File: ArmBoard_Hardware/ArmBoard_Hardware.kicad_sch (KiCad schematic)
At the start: 129 parts, among them J1 RJ45_LED_Shielded, Q1 T2N7002AK,LM, Q10 T2N7002AK,LM, Q11 T2N7002AK,LM, Q2 BSS138, Q3 BSS138, Q4 AO3401A, Q5 T2N7002AK,LM, Q6 T2N7002AK,LM, Q7 T2N7002AK,LM, Q8 T2N7002AK,LM, Q9 T2N7002AK,LM, SW1 SW_Push, SW10 SW_Push, SW12 SW_SPDT, SW2 SW_Push, SW3 SW_Push, SW4 SW_Push, SW5 SW_Push, SW6 SW_Push, SW7 SW_Push, SW8 SW_Push, SW9 SW_Push, U1 PCF8574, U10 PCF8574, U2 OKI, U3 OKI, U4 ATA6561, U5 Teensy4.1_DEV-16771, U6 74HC00, U7 74LS148, U8 74LS148, U9 PCF8574

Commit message: Changes made based on review
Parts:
- removed Q1, Q10, Q11, Q5, Q6, Q7, Q8, Q9: T2N7002AK,LM, Package_TO_SOT_SMD:SOT-23-3, symbol T2N7002AK_LM:T2N7002AK,LM
- removed R28, R30: 4.7k, Resistor_SMD:R_0603_1608Metric_Pad0.98x0.95mm_HandSolder, symbol Device:R
- added Q1, Q10, Q12, Q5, Q6, Q7, Q8, Q9: BSS138, Package_TO_SOT_SMD:SOT-23, symbol Transistor_FET:BSS138
- C6: value 10nF -> 100nF
- R10, R11, R12, R13, R4, R5, R6, R7, R8, R9: value R -> 4.7k
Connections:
- net GND: now also Q1.2 (S), Q10.2 (S), Q12.2 (S), Q5.2 (S), Q6.2 (S), Q7.2 (S), Q8.2 (S), Q9.2 (S)
- net PWM_1: now also Q12.1 (G)
- net PWM_2: now also Q5.1 (G)
- net PWM_3: now also Q1.1 (G)
- net PWM_4: now also Q6.1 (G)
- net PWM_5: now also Q7.1 (G)
- net PWM_6: now also Q8.1 (G)
- net PWM_7: now also Q9.1 (G)
- net PWM_8: now also Q10.1 (G)
- net at D10.1 (K): now also Q7.3 (D)
- net at D13.1 (K): now also Q10.3 (D)
- net at D12.1 (K): now also Q9.3 (D)
- net at D7.1 (K): now also Q5.3 (D)
- net at D4.1 (K): now also Q12.3 (D)
- net at D9.1 (K): now also Q6.3 (D)
- net at D11.1 (K): now also Q8.3 (D)
- net at D8.1 (K): now also Q1.3 (D)
- no-connect marks 16 -> 20
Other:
- moved on the sheet: Conn22, Conn23, Conn25, Conn26, Conn27, Conn3, R16, R17, R18, R19, R20, R21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

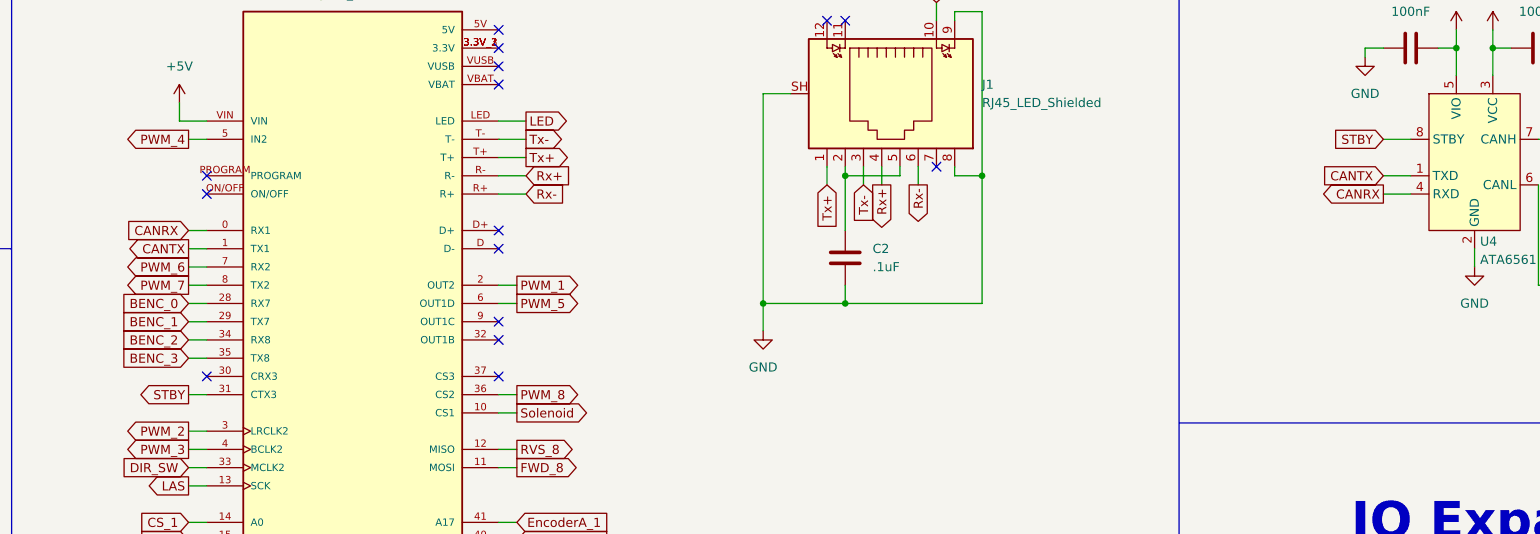
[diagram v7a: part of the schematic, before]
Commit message: Grounded standby on CAN transceiver
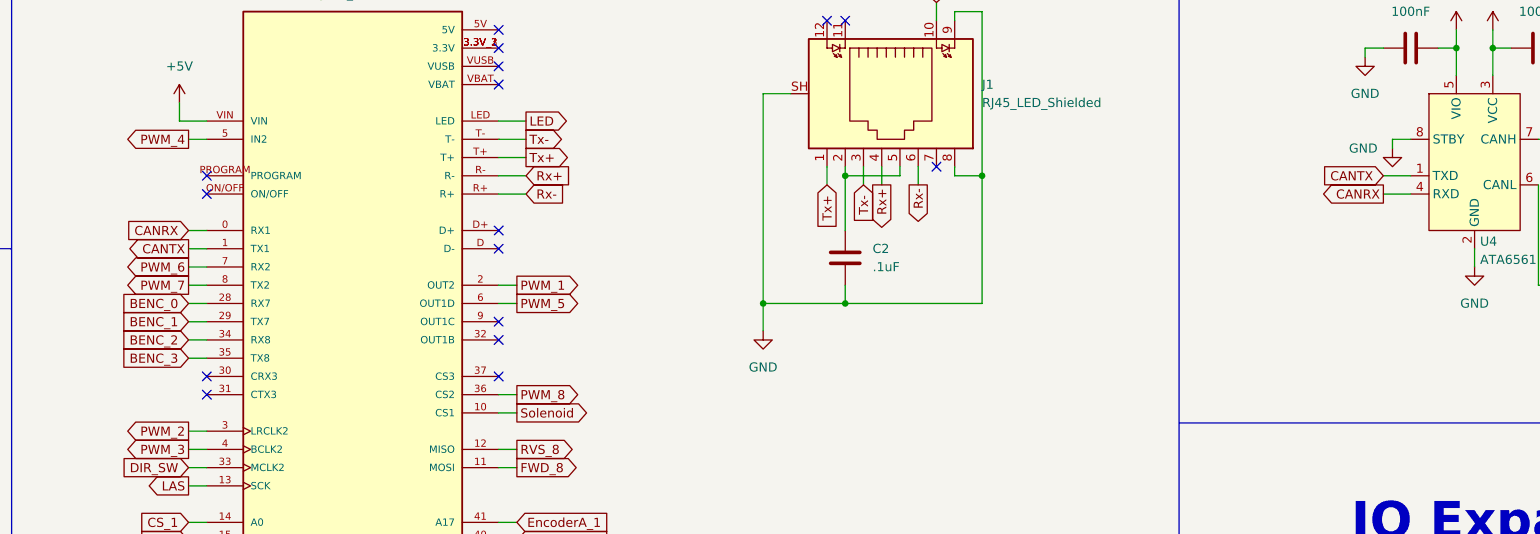
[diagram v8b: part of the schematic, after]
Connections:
- net GND: now also U4.8 (STBY)
- net STBY: no longer names the net of U5.31 (CTX3)
- net STBY: no longer U4.8 (STBY)
- no-connect marks 20 -> 21
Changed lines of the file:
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@@
 	)
 	(no_connect
+		(at 284.48 110.49)
+	)
+	(no_connect
 		(at 373.38 58.42)
 	)
@@
 	(wire
 		(pts
-			(xy 281.94 110.49) (xy 284.48 110.49)
+			(xy 449.58 74.93) (xy 452.12 74.93)
 		)
 		(stroke
@@
 	(wire
 		(pts
+			(xy 449.58 76.2) (xy 449.58 74.93)
+		)
+		(stroke
+			(width 0)
+			(type default)
+		)
+	)
+	(wire
+		(pts
 			(xy 53.34 64.77) (xy 53.34 67.31)
 		)
@@
 	(wire
 		(pts
-			(xy 448.31 74.93) (xy 452.12 74.93)
-		)
-		(stroke
-			(width 0)
-			(type default)
-		)
-	)
-	(wire
-		(pts
 			(xy 260.35 400.05) (xy 262.89 400.05)
 		)
@@
 		)
 	)
-	(global_label "STBY"
-		(shape input)
-		(at 448.31 74.93 180)
-		(fields_autoplaced yes)
-		(effects
-			(font
-				(size 1.27 1.27)
-			)
-			(justify right)
-		)
-		(property "Intersheetrefs" "${INTERSHEET_REFS}"
-			(at 440.7891 74.93 0)
-			(effects
-				(font
-					(size 1.27 1.27)
-				)
-				(justify right)
-				(hide yes)
-			)
-		)
-	)
 	(global_label "CS_6"
 		(shape output)
@@
 		)
 	)
-	(global_label "STBY"
-		(shape output)
-		(at 281.94 110.49 180)
-		(fields_autoplaced yes)
-		(effects
-			(font
-				(size 1.27 1.27)
-			)
-			(justify right)
-		)
-		(property "Intersheetrefs" "${INTERSHEET_REFS}"
-			(at 274.4191 110.49 0)
-			(effects
-				(font
-					(size 1.27 1.27)
-				)
-				(justify right)
-				(hide yes)
-			)
-		)
-	)
 	(global_label "LS_10"
 		(shape input)
@@
 					(unit 1)
 				)
+			)
+		)
+	)
+	(symbol
+		(lib_id "power:GND")
+		(at 449.58 76.2 0)
+		(unit 1)
+		(exclude_from_sim no)
+		(in_bom yes)
+		(on_board yes)
+		(dnp no)
+		(property "Reference" "#PWR0113"
+			(at 449.58 82.55 0)
+			(effects
+				(font
+					(size 1.27 1.27)
+				)
+				(hide yes)
+			)
+		)
+		(property "Value" "GND"
+			(at 445.516 76.2 0)
+			(effects
+				(font
+					(size 1.27 1.27)
+				)
+			)
+		)
+		(property "Footprint" ""
+			(at 449.58 76.2 0)
+			(effects
+				(font
+					(size 1.27 1.27)
+				)
+				(hide yes)
+			)
+		)
+		(property "Datasheet" ""
+			(at 449.58 76.2 0)
+			(effects
+				(font
+					(size 1.27 1.27)
+				)
+				(hide yes)
+			)
+		)
+		(property "Description" "Power symbol creates a global label with name \"GND\" , ground"
+			(at 449.58 76.2 0)
+			(effects
+				(font
+					(size 1.27 1.27)
+				)
+				(hide yes)
+			)
+		)
+		(pin "1"
+		)
+		(instances
+			(project "ArmBoard_Hardware"
+				(path "/45446e72-15bd-4a3c-bc50-99cac403caa6"
+					(reference "#PWR0113")
+					(unit 1)
+				)
